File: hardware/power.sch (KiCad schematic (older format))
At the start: 61 parts, among them P1 CONN_01X02_CBAT, P2 CONN_01X02_FAN, Q1 DMG4712SSS, Q2 DMG4712SSS, SW1 SW-SPST, U10 MCP1501T-30E, U11 PDM1-S, U12 MIC5225-5.0, U7 MIC5225-5.0, U8 LT3471, U9 LF33ABDT

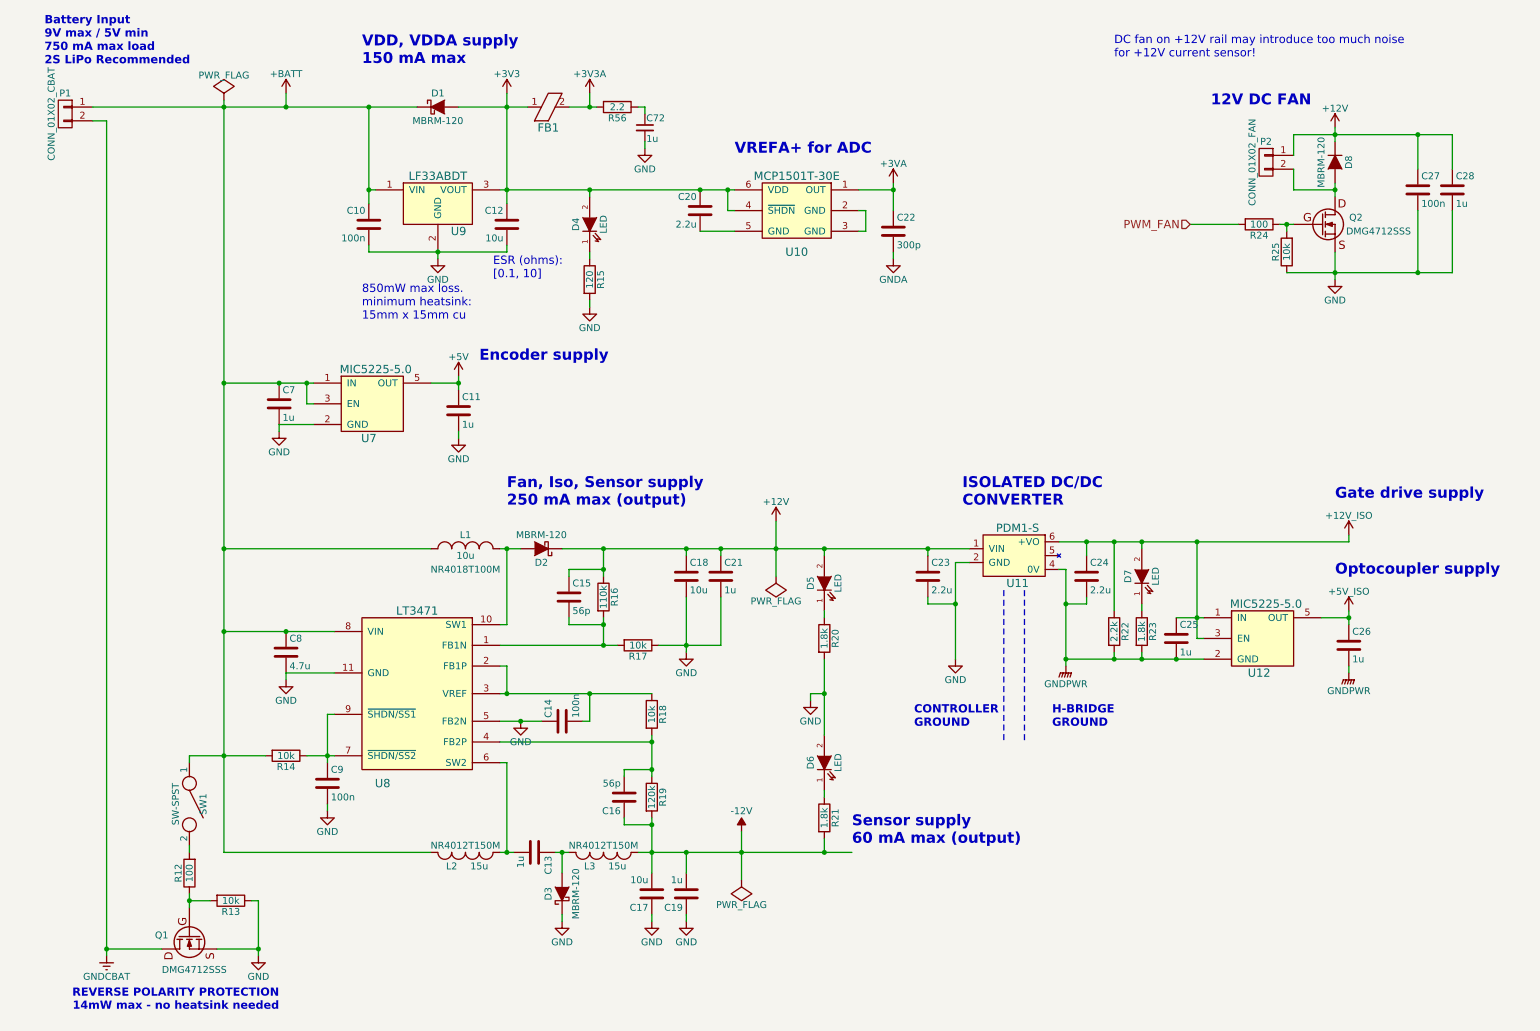
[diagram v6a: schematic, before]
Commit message: Inrush circuit, mounting hole position, temp sensor
- Split inrush circuit (one for each bulk cap). Replaced NTC
  thermistor with 2W power resistor. Replaced D2Pak MOSFET with
  LFPAK MOSFETs.
- Approximate position of mechanical holes chosen.
- Added thermistor temp sensor circuits.
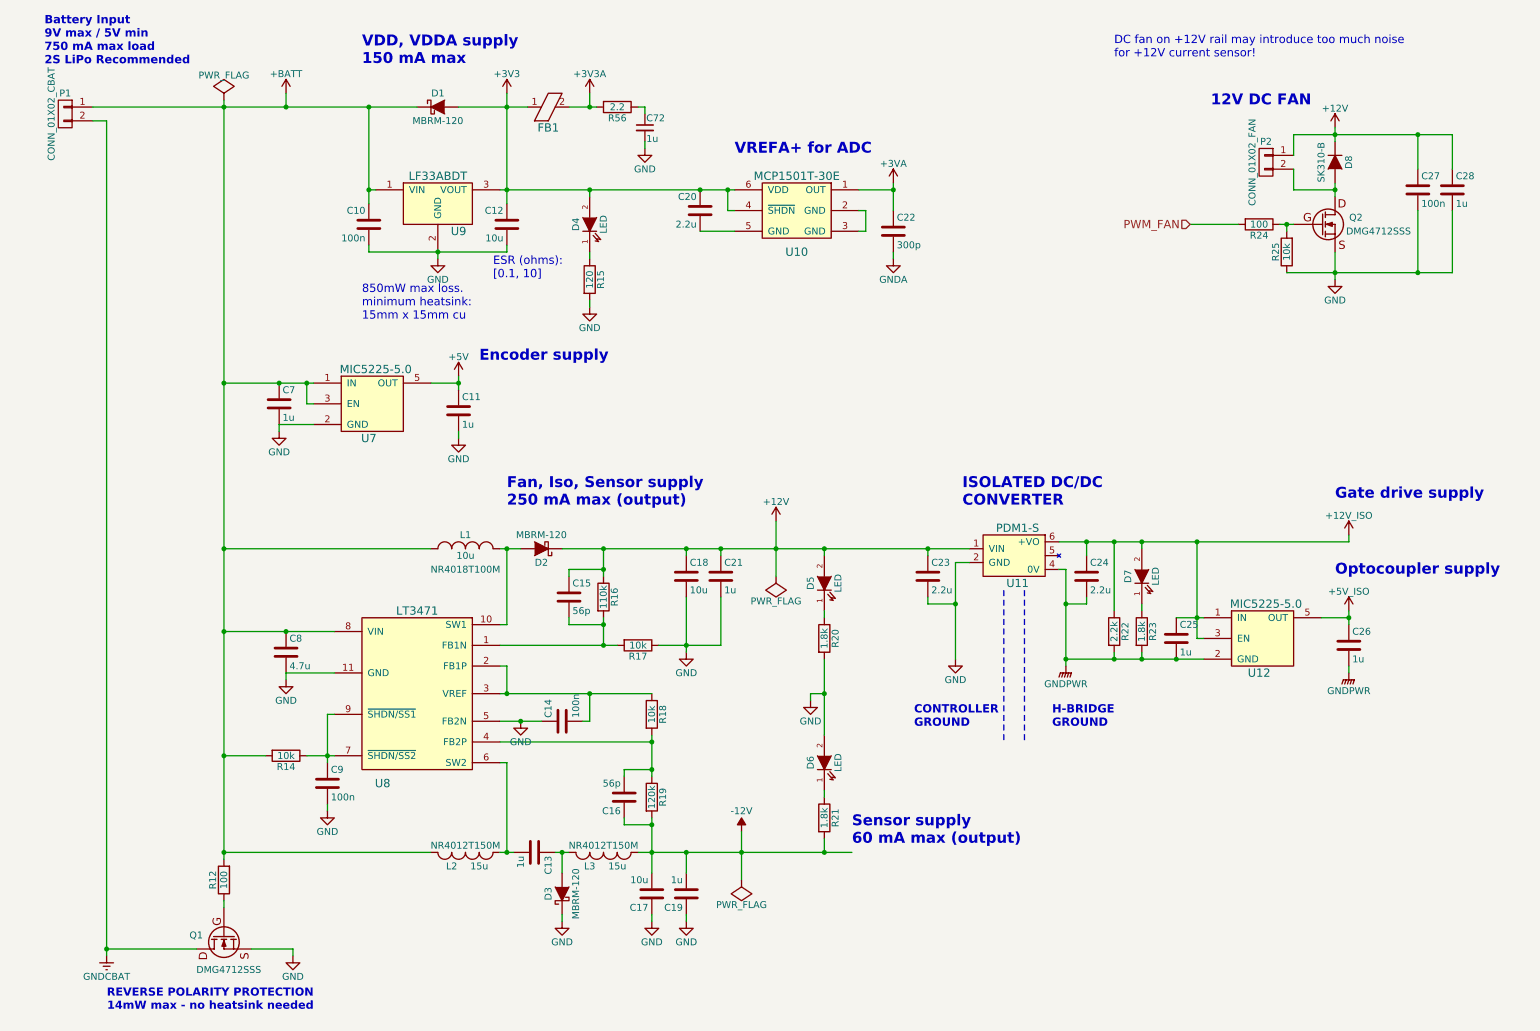
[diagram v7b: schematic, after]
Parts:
- removed R13: 10k, Resistors_SMD:R_0603, symbol R
- removed SW1: SW-SPST, 2kwMotorController:SW_SPST, symbol SW-SPST
- D8: value MBRM-120 -> SK310-B
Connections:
- net +BATT: now also R12.2
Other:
- moved on the sheet: Q1, R12
